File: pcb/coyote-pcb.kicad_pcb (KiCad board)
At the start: 2 copper layers, 106 x 47 mm, 17 parts, among them U1 Basalt

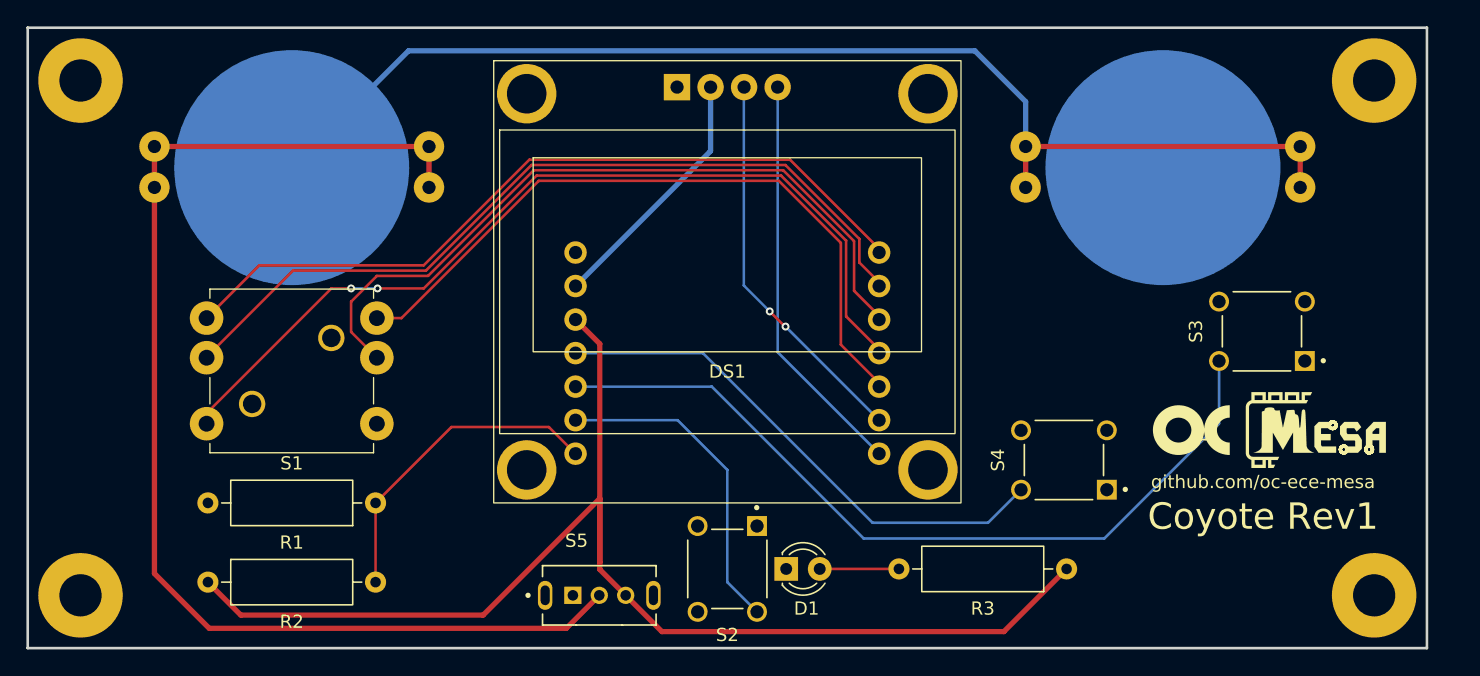
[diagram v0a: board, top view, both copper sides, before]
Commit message: Add dimensional drawing and STEP file
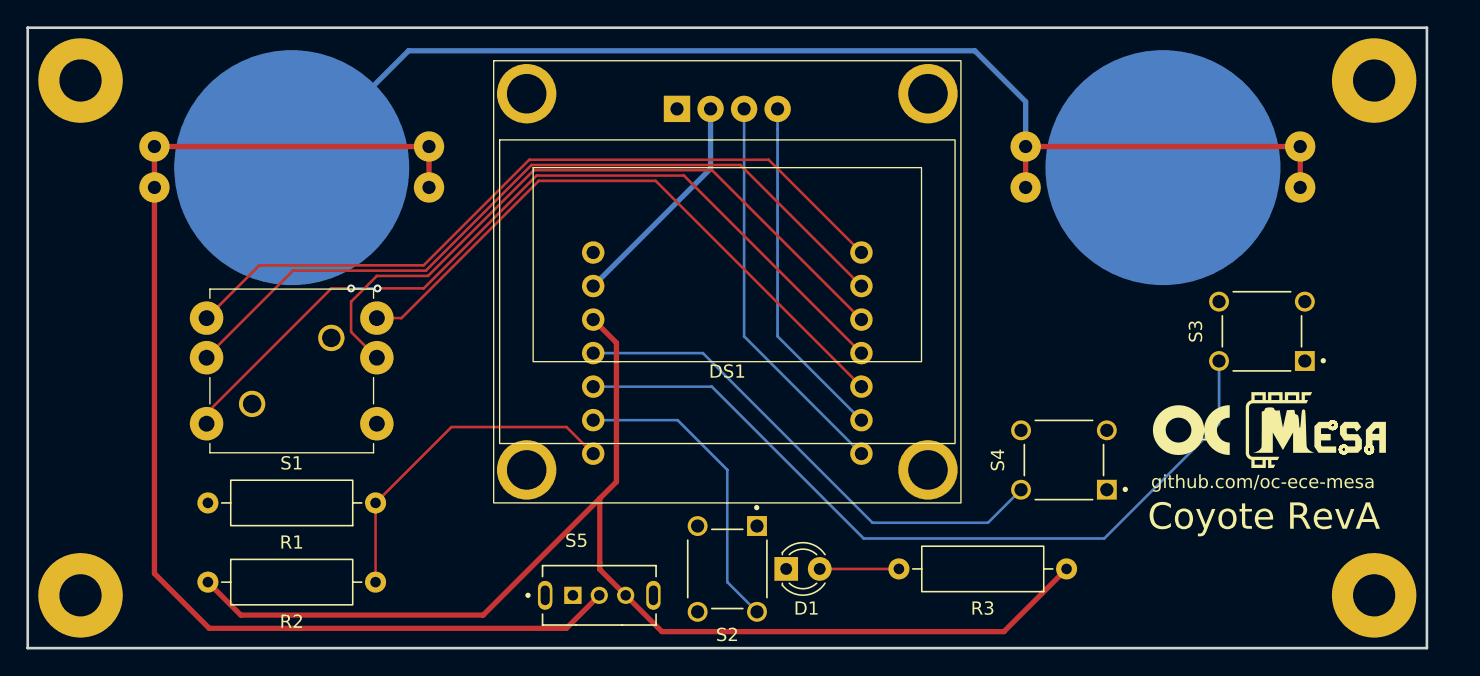
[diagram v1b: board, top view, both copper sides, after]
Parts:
- U1: footprint my-kicad-parts:MESA_Basalt -> my-kicad-parts:MESA_Basalt_RevA
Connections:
- U1 pad 6: Net-(DS1-SCL) -> Net-(DS1-SDA)
- U1 pad 7: Net-(DS1-SDA) -> Net-(DS1-SCL)
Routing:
- net Net-(S1-PRESS): track 53.2 -> 47.5 mm
- net Net-(DS1-SDA): track 31.0 -> 26.2 mm
- net Net-(S1-LEFT): track 69.1 -> 64.5 mm
- net +5V: track 98.5 -> 94.2 mm
- net Net-(S1-DOWN): track 56.0 -> 52.5 mm
- net Net-(S1-RIGHT): track 61.8 -> 59.5 mm
- net +3.3V: track 19.3 -> 17.1 mm
- net Net-(S3-Pad2): track 62.0 -> 60.5 mm
- net Net-(S4-Pad2): track 40.1 -> 38.8 mm
- net Net-(S2-Pad2): track 24.7 -> 23.4 mm
- net Net-(R1-Pad1): track 24.8 -> 26.1 mm
- net Net-(S1-UP): track 58.7 -> 57.5 mm
- net Net-(DS1-SCL): track 29.6 -> 29.8 mm, vias 2 -> 0
